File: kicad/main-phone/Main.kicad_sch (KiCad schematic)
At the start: 0 parts

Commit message: main-phone: free MCU pins; 2x11 spare header with UART and I2C
- LiDAR rail enable joins ~VM-VBAT-EN (PE10); PD9 freed
- IMU FSYNC/INT2 go to J7301 instead of the MCU; FSYNC 100k pull-down (R7601); PD4/PD7 freed
- one open-drain ToF interrupt (PD12) for both VL53L7s and the side VL53L0X; PC8/PE2 freed
- right VL53L7 LPn held up by R7307, no MCU pin; PE8 freed
- IMU moved from I2C2 to I2C4 (R18/R72 not fitted); PA8/PA9 freed;
  R7315 keeps PA9 (UCPD DBCC1) pulled up for dead-battery Rd on CC1
- PWR_EN moved PC10 -> PD7; PC10/PC11 are a spare UART
- J7301 2x6 -> 2x11: 3.3 V, 5 V, I2C4, UART, 12 spare GPIO, IMU FSYNC/INT2, GND
- docs: SPEC, main-phone and side-sensor READMEs

Co-Authored-By: Claude Opus 5.5 <noreply@anthropic.com>
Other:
- sheet FRONT SENSORS ports: added none; removed VL-R-LPn
- sheet MCU-STM32 ports: added none; removed I2C2_SCL, I2C2_SDA, LIDAR_EN, SIDE-PROXI-GPIO-R, VL-R-INT, VL-R-LPn
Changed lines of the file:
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@@
 	(wire
 		(pts
-			(xy 189.23 234.315) (xy 189.23 254.635)
-		)
-		(stroke
-			(width 0)
-			(type default)
-		)
-	)
-	(wire
-		(pts
 			(xy 266.7 146.685) (xy 443.865 146.685)
 		)
@@
 	(wire
 		(pts
-			(xy 186.69 252.095) (xy 100.33 252.095)
+			(xy 110.49 252.095) (xy 100.33 252.095)
 		)
 		(stroke
@@
 	(wire
 		(pts
-			(xy 189.23 254.635) (xy 100.33 254.635)
+			(xy 110.49 254.635) (xy 100.33 254.635)
 		)
 		(stroke
@@
 	(wire
 		(pts
-			(xy 186.69 234.315) (xy 186.69 252.095)
-		)
-		(stroke
-			(width 0)
-			(type default)
-		)
-	)
-	(wire
-		(pts
 			(xy 100.33 207.645) (xy 148.59 207.645)
 		)
@@
 	(wire
 		(pts
-			(xy 231.14 46.355) (xy 231.14 114.3)
-		)
-		(stroke
-			(width 0)
-			(type default)
-		)
-	)
-	(wire
-		(pts
 			(xy 266.7 220.98) (xy 316.865 220.98)
 		)
@@
 	(wire
 		(pts
-			(xy 266.7 201.93) (xy 443.865 201.93)
-		)
-		(stroke
-			(width 0)
-			(type default)
-		)
-	)
-	(wire
-		(pts
 			(xy 245.11 53.34) (xy 239.395 53.34)
 		)
@@
 	(wire
 		(pts
-			(xy 266.7 165.1) (xy 443.865 165.1)
+			(xy 436.88 165.1) (xy 443.865 165.1)
 		)
 		(stroke
@@
 	(wire
 		(pts
-			(xy 266.7 199.39) (xy 443.865 199.39)
+			(xy 440.055 199.39) (xy 443.865 199.39)
 		)
 		(stroke
@@
 		)
 	)
-	(label "VL-R-INT"
+	(label "VL-L-INT"
 		(at 440.055 199.39 180)
 		(effects
@@
 		)
 	)
-	(label "VL-R-LPn"
-		(at 270.51 201.93 0)
-		(effects
-			(font
-				(size 1.27 1.27)
-			)
-			(justify left bottom)
-		)
-	)
 	(label "USB_VBUS_SENSE"
 		(at 287.02 220.98 180)
@@
 		)
 	)
-	(label "VL-R-INT"
-		(at 270.51 199.39 0)
-		(effects
-			(font
-				(size 1.27 1.27)
-			)
-			(justify left bottom)
-		)
-	)
 	(label "USB_CC2"
 		(at 299.72 345.44 0)
@@
 		)
 	)
-	(label "VL-R-LPn"
-		(at 440.055 201.93 180)
-		(effects
-			(font
-				(size 1.27 1.27)
-			)
-			(justify right bottom)
-		)
-	)
 	(sheet
 		(at 240.03 275.59)
@@
 			)
 		)
-		(pin "VL-R-LPn" output
-			(at 266.7 201.93 0)
-			(effects
-				(font
-					(size 1.27 1.27)
-				)
-				(justify right)
-			)
-		)
 		(pin "LiDAR-M-CTRL" output
 			(at 266.7 162.56 0)
@@
 			)
 		)
-		(pin "SIDE-PROXI-GPIO-R" input
-			(at 231.14 114.3 90)
-			(effects
-				(font
-					(size 1.27 1.27)
-				)
-				(justify right)
-			)
-		)
-		(pin "LIDAR_EN" output
-			(at 266.7 165.1 0)
-			(effects
-				(font
-					(size 1.27 1.27)
-				)
-				(justify right)
-			)
-		)
 		(pin "WDI" output
 			(at 266.7 146.685 0)
@@
 			)
 		)
-		(pin "I2C2_SCL" output
-			(at 189.23 234.315 270)
-			(effects
-				(font
-					(size 1.27 1.27)
-				)
-				(justify left)
-			)
-		)
-		(pin "I2C2_SDA" bidirectional
-			(at 186.69 234.315 270)
-			(effects
-				(font
-					(size 1.27 1.27)
-				)
-				(justify left)
-			)
-		)
 		(pin "DM" bidirectional
 			(at 215.265 234.315 270)
@@
 			)
 		)
-		(pin "VL-R-INT" input
-			(at 266.7 199.39 0)
-			(effects
-				(font
-					(size 1.27 1.27)
-				)
-				(justify right)
-			)
-		)
 		(instances
 			(project "Main"
@@
 			)
 		)
-		(pin "VL-R-LPn" input
-			(at 443.865 201.93 180)
-			(effects
-				(font
-					(size 1.27 1.27)
-				)
-				(justify left)
-			)
-		)
 		(pin "IR-F-RX1" output
 			(at 443.865 180.34 180)
@@
 	)
 	(embedded_fonts no)
+	(label "~{VM-VBAT-EN}"
+		(at 436.88 165.1 180)
+		(effects
+			(font
+				(size 1.27 1.27)
+			)
+			(justify right bottom)
+		)
+	)
+	(label "VL-L-INT"
+		(at 231.14 46.355 0)
+		(effects
+			(font
+				(size 1.27 1.27)
+			)
+			(justify left bottom)
+		)
+	)
+	(label "I2C4_SCL"
+		(at 110.49 254.635 0)
+		(effects
+			(font
+				(size 1.27 1.27)
+			)
+			(justify left bottom)
+		)
+	)
+	(label "I2C4_SDA"
+		(at 110.49 252.095 0)
+		(effects
+			(font
+				(size 1.27 1.27)
+			)
+			(justify left bottom)
+		)
+	)
 )

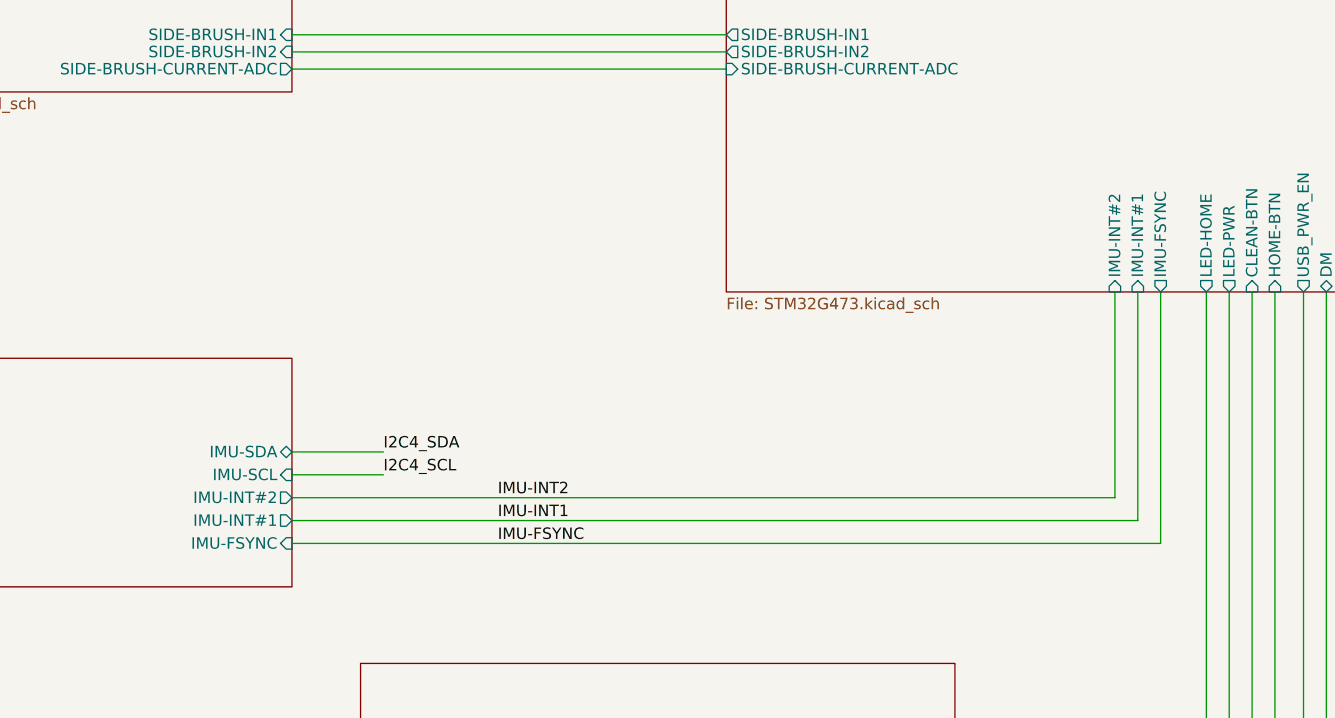
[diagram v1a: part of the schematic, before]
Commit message: Per-board reference ranges, J1 spare header, IMU AD0 pull-down, BOM outputs
- reference ranges: main-phone 1-999, dock 1000s, front ToF 2000s, side 3000s,
  cliff 4000s, rear IR 5000s, Hall 6000s (main-phone 7xxx parts renumbered
  below 1000; sensor boards and dock moved from 8xxx)
- main-phone: J7301 -> J1, a fitted 2x7 0.1" header with spares only
  (3.3 V, 5 V, I2C4, UART PC10/PC11, PA8-PA10, PD4, PE2, PE6, GND)
- IMU: AP_AD0 pulled low by R217 (address 0x68); INT2 on test pad TP1;
  FSYNC reachable on R211; R18/R72 removed
- tools/export.py replaces export_pdfs.py: schematic PDF and JLC-style BOM in
  each board's output/ folder; --pcb adds Gerbers, placement and STEP
- cliff and rear IR projects: fix top-level sheet left over from a copy
- Hall board: visual tidy-up

Co-Authored-By: Claude Opus 5.5 <noreply@anthropic.com>
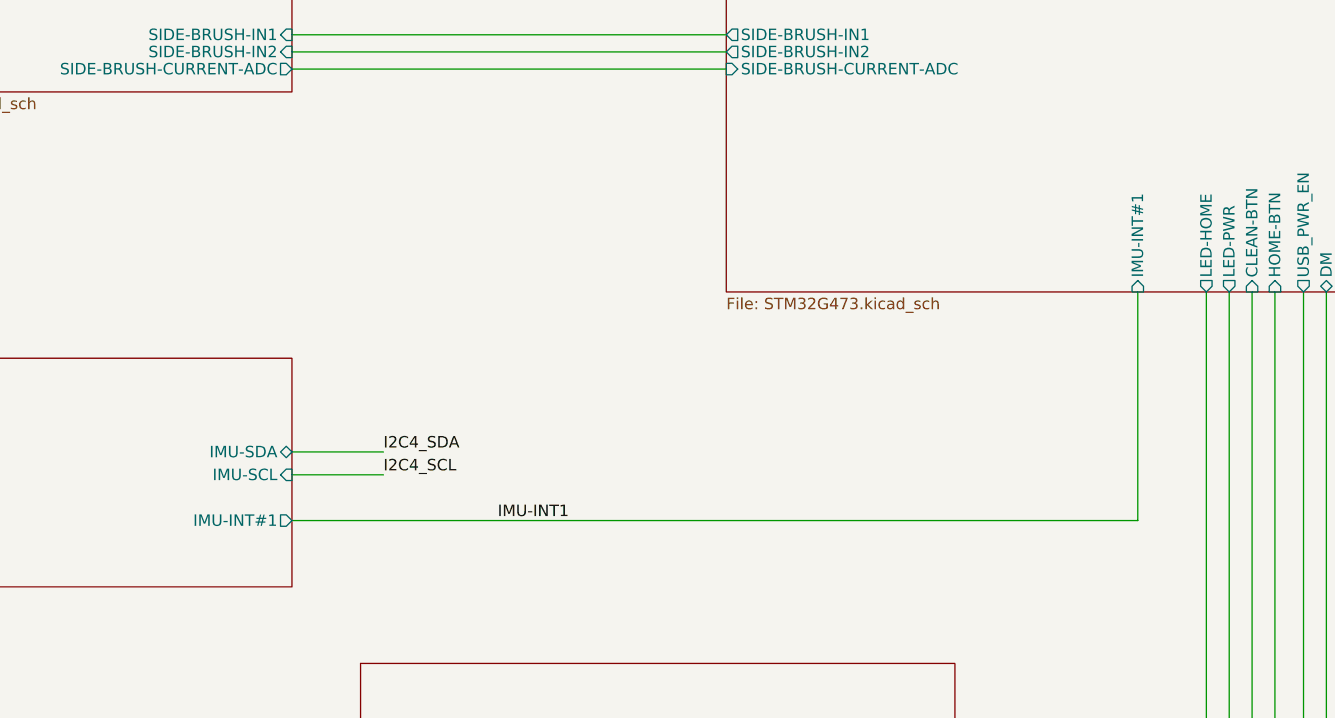
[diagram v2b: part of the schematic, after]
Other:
- sheet IMU ports: added none; removed IMU-FSYNC, IMU-INT#2
- sheet MCU-STM32 ports: added none; removed IMU-FSYNC, IMU-INT#2
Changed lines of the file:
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@@
-	(wire
-		(pts
-			(xy 100.33 262.255) (xy 196.85 262.255)
-		)
-		(stroke
-			(width 0)
-			(type default)
-		)
-	)
 	(wire
 		(pts
@@
 	(wire
 		(pts
-			(xy 191.77 234.315) (xy 191.77 257.175)
-		)
-		(stroke
-			(width 0)
-			(type default)
-		)
-	)
-	(wire
-		(pts
-			(xy 100.33 257.175) (xy 191.77 257.175)
-		)
-		(stroke
-			(width 0)
-			(type default)
-		)
-	)
-	(wire
-		(pts
 			(xy 179.07 42.545) (xy 210.82 42.545)
 		)
@@
 		(pts
 			(xy 100.33 116.205) (xy 119.38 116.205)
-		)
-		(stroke
-			(width 0)
-			(type default)
-		)
-	)
-	(wire
-		(pts
-			(xy 196.85 234.315) (xy 196.85 262.255)
 		)
 		(stroke
@@
 		)
 	)
-	(label "IMU-FSYNC"
-		(at 123.19 262.255 0)
-		(effects
-			(font
-				(size 1.27 1.27)
-			)
-			(justify left bottom)
-		)
-	)
 	(label "VL-L-LPn"
 		(at 440.055 196.85 180)
@@
 	(label "I2C4_SDA"
 		(at 236.855 114.3 90)
-		(effects
-			(font
-				(size 1.27 1.27)
-			)
-			(justify left bottom)
-		)
-	)
-	(label "IMU-INT2"
-		(at 123.19 257.175 0)
 		(effects
 			(font
@@
 			)
 		)
-		(pin "IMU-INT#2" input
-			(at 191.77 234.315 270)
-			(effects
-				(font
-					(size 1.27 1.27)
-				)
-				(justify left)
-			)
-		)
 		(pin "IMU-INT#1" input
 			(at 194.31 234.315 270)
-			(effects
-				(font
-					(size 1.27 1.27)
-				)
-				(justify left)
-			)
-		)
-		(pin "IMU-FSYNC" output
-			(at 196.85 234.315 270)
 			(effects
 				(font
@@
 			)
 		)
-		(pin "IMU-INT#2" output
-			(at 100.33 257.175 0)
-			(effects
-				(font
-					(size 1.27 1.27)
-				)
-				(justify right)
-			)
-		)
 		(pin "IMU-INT#1" output
 			(at 100.33 259.715 0)
 			(effects
 				(font
-					(size 1.27 1.27)
-				)
-				(justify right)
-			)
-		)
-		(pin "IMU-FSYNC" input
-			(at 100.33 262.255 0)
-			(effects
-				(font
